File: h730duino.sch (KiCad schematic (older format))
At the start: 72 parts, among them J4 105162-0001, J7 Conn_02x03_Odd_Even, P1 Digital, P10 CONN_01X01, P11 CONN_01X01, P13 CONN_01X01, P2 Power, P3 Analog, P4 Analog, P5 PWM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

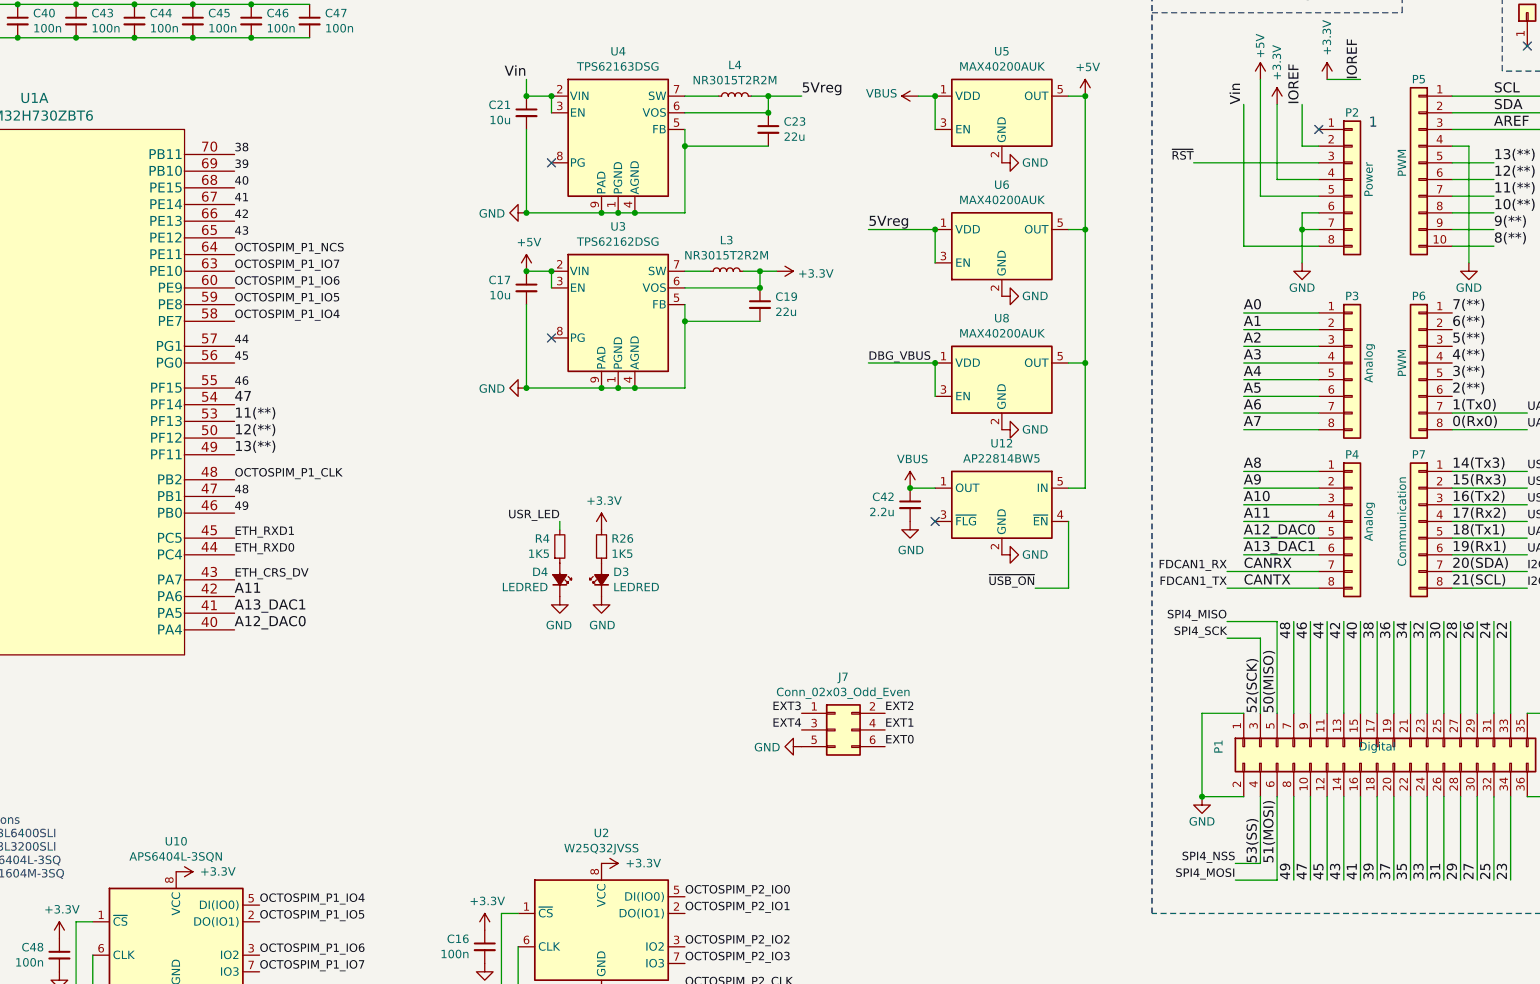
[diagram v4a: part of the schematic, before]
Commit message: Add new BOM to octopart
TODO: PSRAM is not recognized by Octopart but is available in LCSC

Signed-off-by: Martin Ribelotta <martinribelotta@gmail.com>
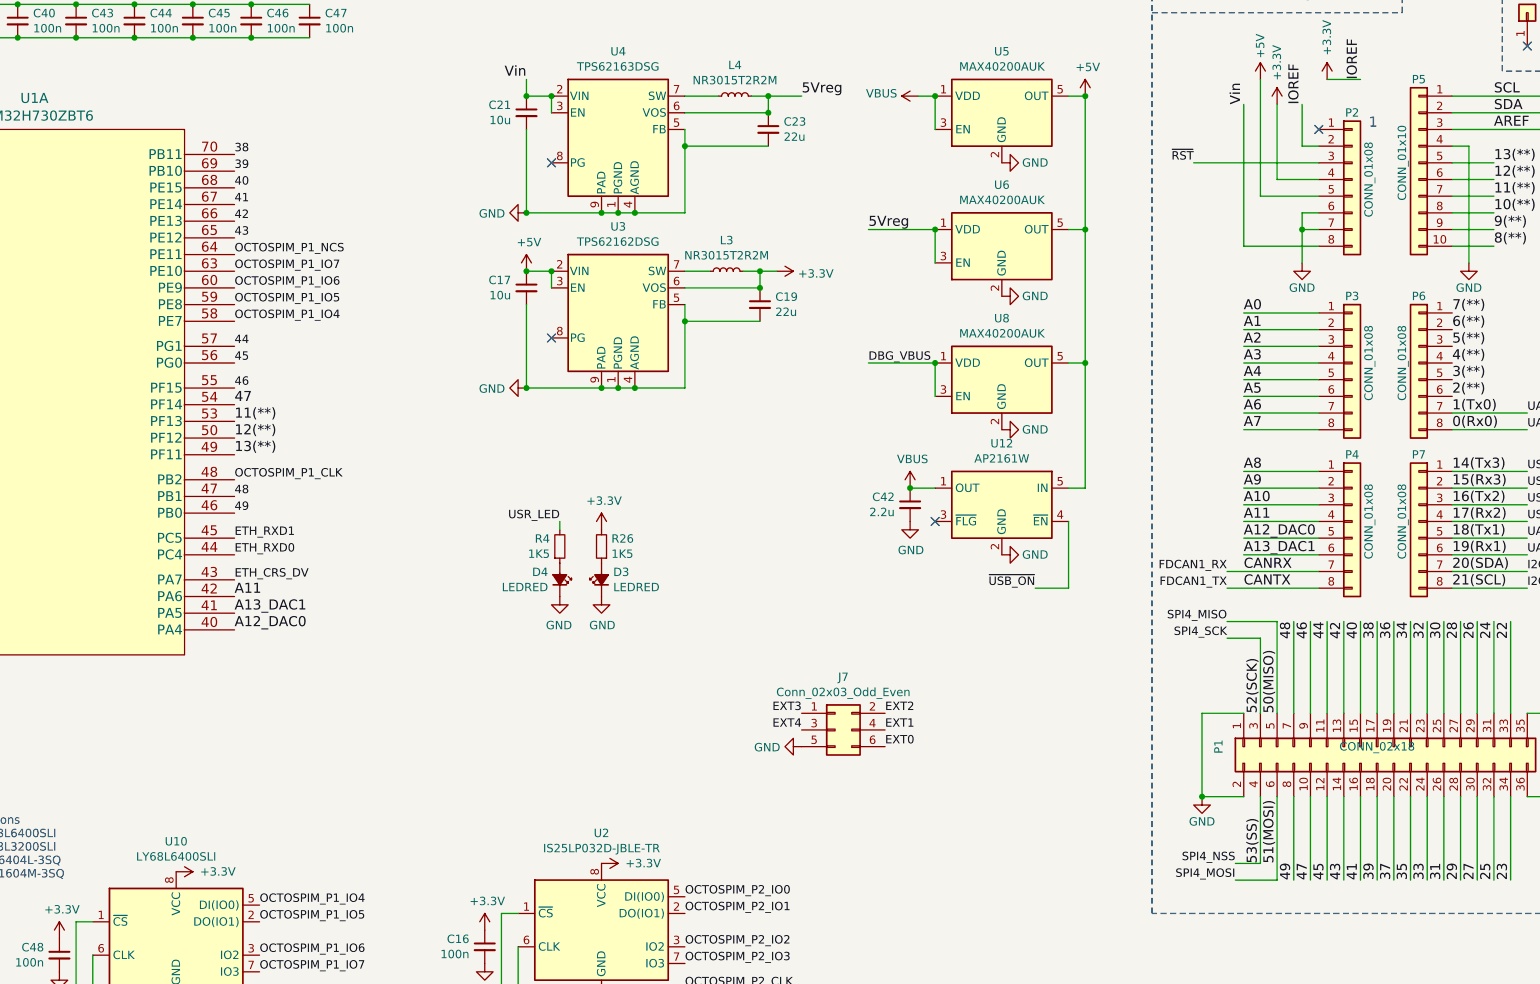
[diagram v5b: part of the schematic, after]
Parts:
- removed U12: AP22814BW5, Package_TO_SOT_SMD:SOT-23-5, symbol Power_Management:AP22814BW5
- added U12: AP2161W, Package_TO_SOT_SMD:SOT-23-5, symbol Power_Management:AP2161W
- C1: MANUFACTURER (none) -> Yageo; MANUFACTURER_PART_NUMBER (none) -> CC0603KRX5R5BB475
- C10, C12: MANUFACTURER (none) -> Yageo; MANUFACTURER_PART_NUMBER (none) -> CC0603CRNPO9BN1R0
- C11, C8, C9: MANUFACTURER (none) -> Yageo; MANUFACTURER_PART_NUMBER (none) -> CC0603JRNPO9BN100
- C13: MANUFACTURER (none) -> Yageo; MANUFACTURER_PART_NUMBER (none) -> CC0603ZRY5V6BB105
- C14, C15, C42: MANUFACTURER (none) -> Yageo; MANUFACTURER_PART_NUMBER (none) -> CC0603ZRY5V6BB225
- C16, C2, C3, C39, C4, C40, C41, C43, C44, C45, C46, C47, C48, C5, C6, C7: MANUFACTURER (none) -> Yageo; MANUFACTURER_PART_NUMBER (none) -> CC0603KRX7R9BB104
- C17, C21: MANUFACTURER (none) -> AVX; MANUFACTURER_PART_NUMBER (none) -> 0603ZD106KAT2A
- C19, C23: MANUFACTURER (none) -> Murate; MANUFACTURER_PART_NUMBER (none) -> GRM188R61A226ME15D
- D3, D4: MANUFACTURER (none) -> Osram; MANUFACTURER_PART_NUMBER (none) -> LS Q976-NR-1
- J4: MANUFACTURER (none) -> Molex
- L1: MANUFACTURER (none) -> Taiyo Yuden; MANUFACTURER_PART_NUMBER (none) -> BK1608HS220-T
- L3, L4: MANUFACTURER (none) -> Taiyo Yuden; MANUFACTURER_PART_NUMBER (none) -> NR3015T2R2M
- P1: value Digital -> CONN_02x18; MANUFACTURER (none) -> Oupiin; MANUFACTURER_PART_NUMBER (none) -> 2044-2X18G00SA
- P2: value Power -> CONN_01x08; MANUFACTURER (none) -> Oupin; MANUFACTURER_PART_NUMBER (none) -> 2044-1X08G00SA
- P3, P4: value Analog -> CONN_01x08; MANUFACTURER (none) -> Oupin; MANUFACTURER_PART_NUMBER (none) -> 2044-1X08G00SA
- P5: value PWM -> CONN_01x10; MANUFACTURER (none) -> Oupin; MANUFACTURER_PART_NUMBER (none) -> 2044-1X10G00SA
- P6: value PWM -> CONN_01x08; MANUFACTURER (none) -> Oupin; MANUFACTURER_PART_NUMBER (none) -> 2044-1X08G00SA
- P7: value Communication -> CONN_01x08; MANUFACTURER (none) -> Oupin; MANUFACTURER_PART_NUMBER (none) -> 2044-1X08G00SA
- R20, R27, R28, R29, R30, R31, R5: MANUFACTURER (none) -> Yageo; MANUFACTURER_PART_NUMBER (none) -> RC0603FR-0710KL
- R26, R4: MANUFACTURER (none) -> Yageo; MANUFACTURER_PART_NUMBER (none) -> RC0603JR-071K5L
- SW1: MANUFACTURER (none) -> C&K; MANUFACTURER_PART_NUMBER (none) -> PTS645VL58-2 LFS
- U1: MANUFACTURER (none) -> ST; MANUFACTURER_PART_NUMBER (none) -> STM32H730ZBT6
- U10: value APS6404L-3SQN -> LY68L6400SLI; MANUFACTURER (none) -> Lyontek; MANUFACTURER_PART_NUMBER (none) -> LY68L6400SLI
- U2: value W25Q32JVSS -> IS25LP032D-JBLE-TR; MANUFACTURER (none) -> ISSI; MANUFACTURER_PART_NUMBER (none) -> IS25LP032D-JBLE-TR
- U3: MANUFACTURER (none) -> TI; MANUFACTURER_PART_NUMBER (none) -> TPS62162DSG
- U4: MANUFACTURER (none) -> TI; MANUFACTURER_PART_NUMBER (none) -> TPS62163DSG
- U5, U6, U8: MANUFACTURER (none) -> Maxim; MANUFACTURER_PART_NUMBER (none) -> MAX40200AUK
- Y1: MANUFACTURER (none) -> QST; MANUFACTURER_PART_NUMBER (none) -> QT3C-32.768KDZF-T
- Y2: MANUFACTURER (none) -> Abracon; MANUFACTURER_PART_NUMBER (none) -> ABM7-8.000MHZ-D2Y-T
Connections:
- net +5V: now also U12.5 (IN)
- net GND: now also U12.2 (GND)
- net VBUS: now also U12.1 (OUT)
- net ~USB_ON: now also U12.4 (~EN)

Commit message: Update schemas
Signed-off-by: Martin Ribelotta <martinribelotta@gmail.com>
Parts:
- Y1: MANUFACTURER QST -> Citizen Finedevice; MANUFACTURER_PART_NUMBER QT3C-32.768KDZF-T -> CM315D32768DZFT
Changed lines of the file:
@@
 F 3 "~" H 1050 1100 50  0001 C CNN
 F 4 "Crystal 32.768KHz 3215" H 1050 1100 50  0001 C CNN "DESCRIPTION"
-F 5 "QST" H 1050 1100 50  0001 C CNN "MANUFACTURER"
-F 6 "QT3C-32.768KDZF-T" H 1050 1100 50  0001 C CNN "MANUFACTURER_PART_NUMBER"
+F 5 "Citizen Finedevice " H 1050 1100 50  0001 C CNN "MANUFACTURER"
+F 6 "CM315D32768DZFT" H 1050 1100 50  0001 C CNN "MANUFACTURER_PART_NUMBER"
 	1    1050 1100
 	1    0    0    -1

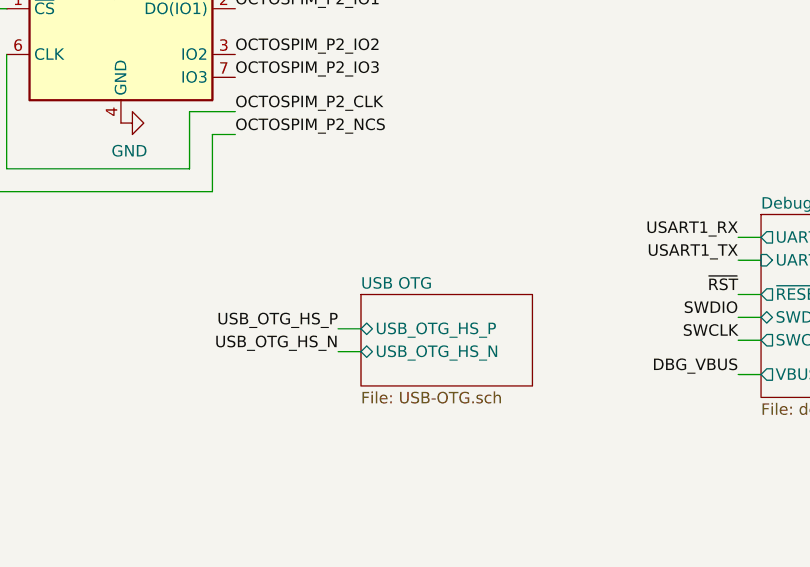
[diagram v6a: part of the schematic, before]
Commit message: Replace STM32F042 in TSSOP by STM32F04[28] in QFN28
Others changes:

 - Export gerbers to current status
 - Update schematic export in svg and pdf
 - Update README image
 - Rename `USB OTG` sheet to `USB_OTG`

Signed-off-by: Martin Ribelotta <martinribelotta@gmail.com>
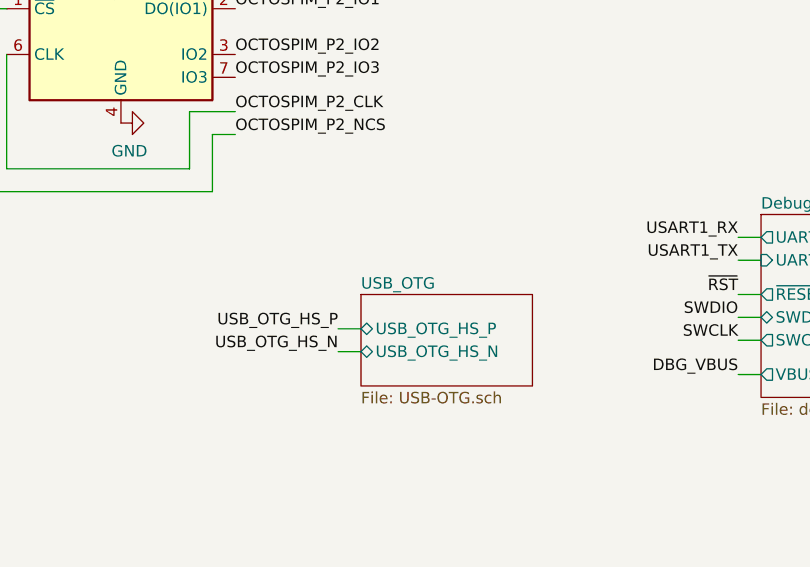
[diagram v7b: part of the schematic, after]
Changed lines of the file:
@@
 S 10950 7300 750  400
 U 604C2CA4
-F0 "USB OTG" 50
+F0 "USB_OTG" 50
 F1 "USB-OTG.sch" 50
 F2 "USB_OTG_HS_P" B L 10950 7450 50
